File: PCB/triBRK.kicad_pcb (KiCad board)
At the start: 2 copper layers, 60.9 x 43.2 mm, 11 parts, among them SW1 SW_Push, SW2 SW_Push, SW3 SW_Push, SW4 SW_Push, SW5 SW_Push, U1 YAAJ_BluePill_Part_Like

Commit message: Small changes
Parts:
- moved H1 0.51 mm to (184.4, 53.6)
- moved SW1 0.46 mm to (186.7, 57.1)
- moved SW2 0.31 mm to (186.7, 43.4)
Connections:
- U1 pad 38: +3.3V -> unconnected-(U1-Pad38)
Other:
- board text added: "v0.1"

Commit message: corrected typo
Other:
- board text added: "triBRK three Button Rhythm Keyboard by Vlad Hațegan"
- board text removed: "triBRK three button rythm keyboard by Vlad Hațegan"
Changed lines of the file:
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@@
       (drillshape 0)
       (scaleselection 1)
-      (outputdirectory "/home/vhateg/Downloads/")
+      (outputdirectory "/home/vhateg/Downloads/gerber_v0.1/")
     )
   )
@@
   )
   (gr_rect (start 188.214 85.09) (end 127.350384 41.91) (layer "Edge.Cuts") (width 0.15) (fill none))
-  (gr_text "triBRK\n\nthree button rythm keyboard\nby Vlad Hațegan" (at 157.48 61.976) (layer "B.SilkS")
+  (gr_text "triBRK\n\nthree Button Rhythm Keyboard\nby Vlad Hațegan" (at 157.48 61.976) (layer "B.SilkS")
     (effects (font (size 2 2) (thickness 0.3)) (justify mirror))
   )

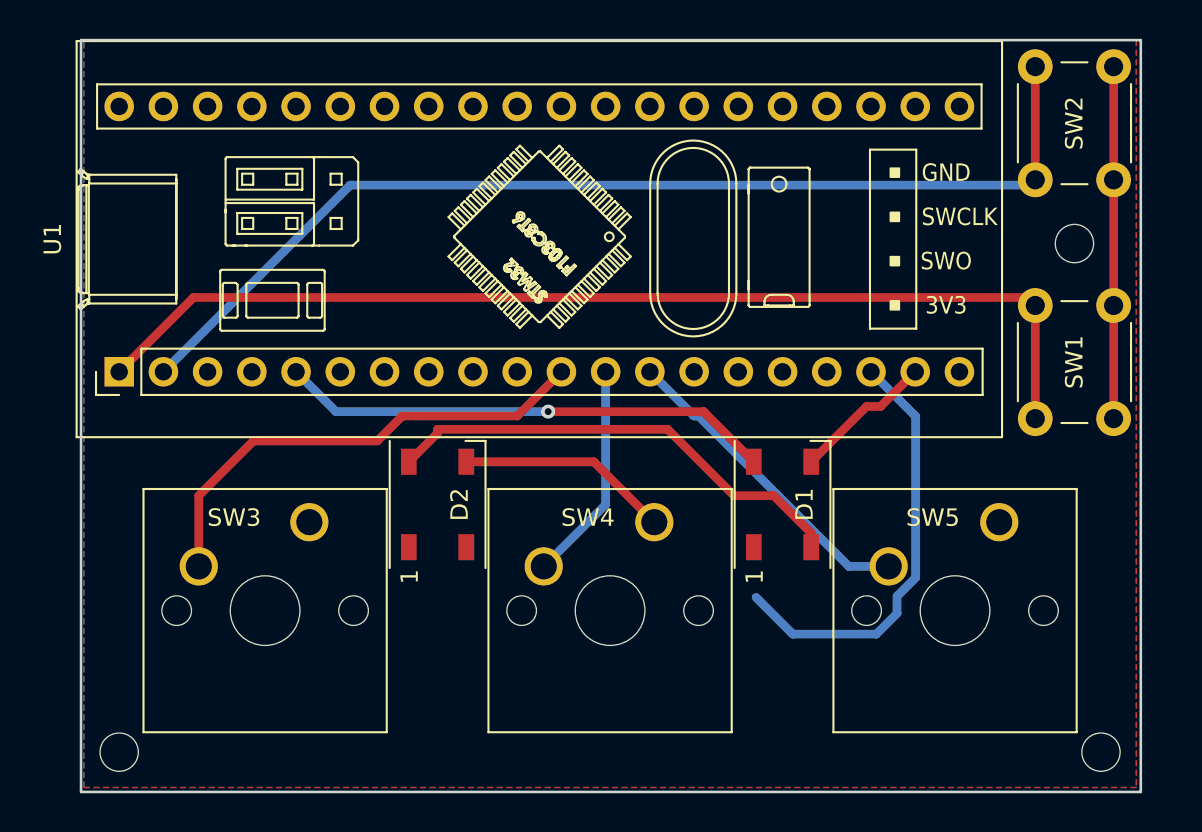
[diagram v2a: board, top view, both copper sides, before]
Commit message: Rounder corners + other optimisations
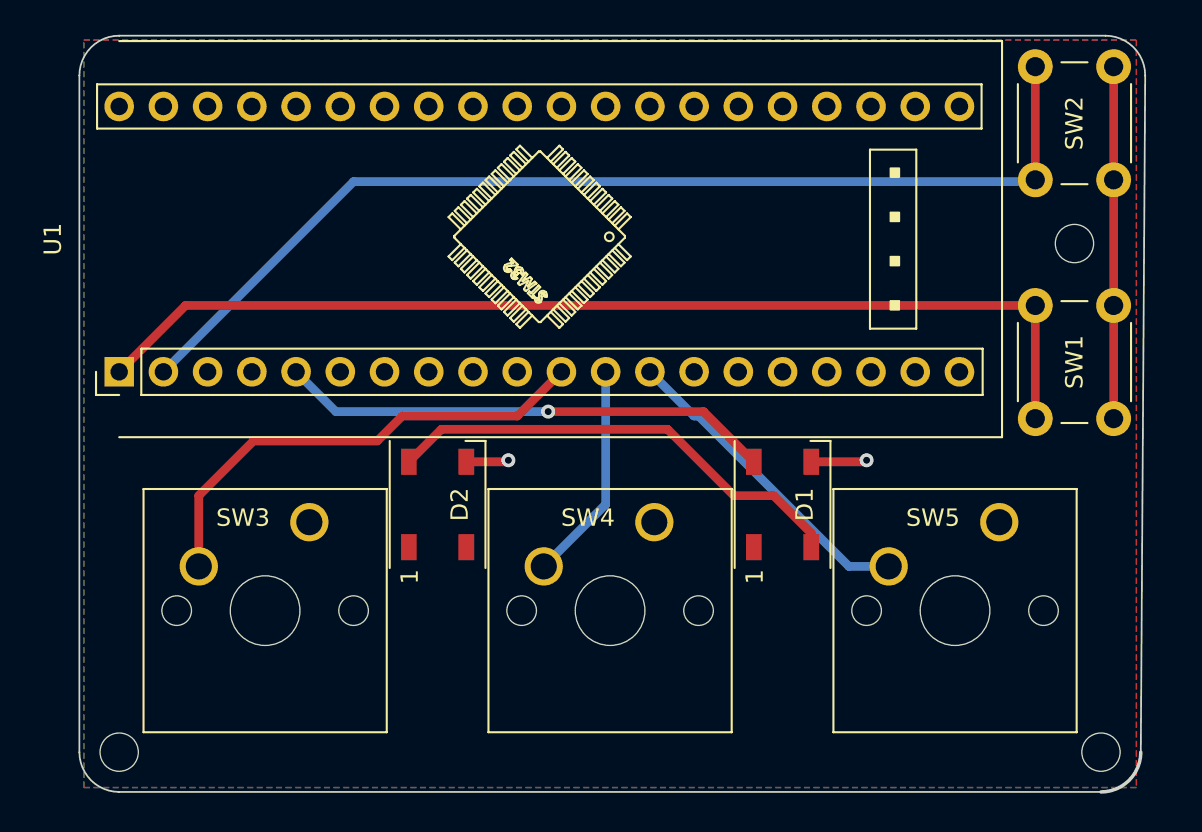
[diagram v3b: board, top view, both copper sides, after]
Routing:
- net +5V: track 25.0 -> 0.18 mm
- net GND: track 40.2 -> 25.5 mm, vias 0 -> 2
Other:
- board size 60.9 x 43.2 mm -> 61.2 x 43.4 mm
- board text added: "v0.1.1"
- board text removed: "v0.1"

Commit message: Changed holes specs and optimized wiring, nicer schematic also
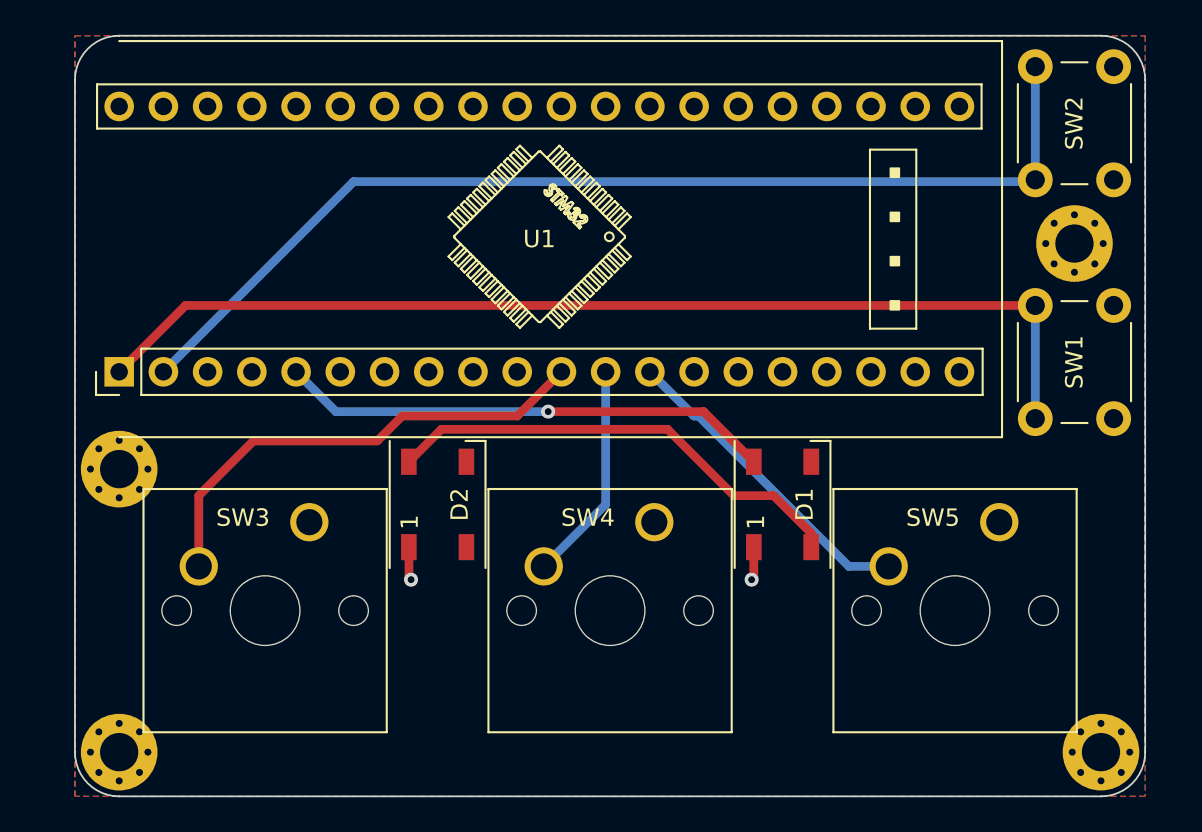
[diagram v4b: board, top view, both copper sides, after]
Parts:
- added H4: MountingHole, MountingHole:MountingHole_2.2mm_M2_Pad_Via, F.Cu at (129.5, 66.5)
- H1, H2, H3: footprint MountingHole:MountingHole_2.2mm_M2_ISO7380 -> MountingHole:MountingHole_2.2mm_M2_Pad_Via
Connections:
- net Net-(D1-Pad4) renamed LEDS
- net Net-(SW1-Pad2) renamed B1
- net Net-(SW2-Pad2) renamed B2
- net Net-(SW3-Pad2) renamed SW1
- net Net-(SW4-Pad2) renamed SW2
- net Net-(SW5-Pad2) renamed SW3
- U1 pad 20: +3.3V -> unconnected-(U1-Pad20)
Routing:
- net GND: track 25.5 -> 0.00 mm, vias 2 -> 0
- net +5V: track 0.18 -> 3.84 mm, vias 0 -> 2
- added copper zone on B.Cu, net +5V
- added copper zone on F.Cu, net GND
- removed copper zone on F.Cu, net +5V
- removed copper zone on B.Cu, net GND
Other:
- board size 61.2 x 43.4 mm -> 61.5 x 43.7 mm
- board text added: "v0.1"
- board text removed: "v0.1.1"
